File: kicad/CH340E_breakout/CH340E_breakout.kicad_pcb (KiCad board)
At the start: 2 copper layers, 22.7 x 16.7 mm, 27 parts, among them J1 USB-ID, J2 FTDI_PINS_1X06_input, U1 MCP1702-CB, U2 HT42B534-MSOP10

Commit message: schematic and routing completed
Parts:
- removed C10, C9: 47p, SquantorRcl:C_0402
- removed C6: 100n, SquantorRcl:C_0402
- removed R4, R5: 33, SquantorRcl:R_0402_hand
- removed R8: 10K, SquantorRcl:R_0402_hand
- removed SJ1: vddio=vddconn, SquantorSpecial:solder_jumper_2way_noconn
- removed SJ3: vddio=3.3v, SquantorSpecial:solder_jumper_2way_conn
- added R2: 1K, SquantorRcl:R_0402_hand, F.Cu at (152.7, 97.8)
- D2: value D_Schottky -> RED; footprint SquantorDiodes:SOD-523 -> SquantorRcl:R_0603_hand
- U2: value HT42B534-MSOP10 -> CH340E
- moved N1 14.2 mm to (136.4, 86.1)
- moved N2 14.2 mm to (135.3, 90.1)
- moved D2 12.4 mm to (150.0, 97.8)
- moved D1 12.0 mm to (151.7, 85.4)
- moved R6 11.7 mm to (149.5, 85.5), turned to 270 degrees
- moved C7 6.23 mm to (149.9, 89.3), turned to 180 degrees
- moved C4 2.95 mm to (153.3, 95.2)
- moved SJ2 2.95 mm to (150.9, 95.3)
- moved U1 2.95 mm to (150.5, 95.3)
- moved U2 2.86 mm to (150.1, 91.8), turned to 0 degrees
- moved J2 2.60 mm to (157.5, 97.3)
- moved C8 2.23 mm to (152.5, 89.2), turned to 180 degrees
- moved R1 0.81 mm to (147.8, 94.8), turned to 270 degrees
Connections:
- D2 pad 1: /VDD -> /VSS
- D2 pad 2: /VDDIO -> Net-(D2-Pad2)
- U2 pad 1: /VDD -> /USB_DP
- U2 pad 10: Net-(C10-Pad2) -> /VDD_33V
- U2 pad 2: /VDD_33V -> /USB_DM
- U2 pad 4: /CTSI -> /RTSO
- U2 pad 5: /TXO -> /CTSI
- U2 pad 6: /VDDIO -> /ACT
- U2 pad 7: /RXI -> /VDD
- U2 pad 8: /RTSO -> /TXO
- U2 pad 9: Net-(C9-Pad2) -> /RXI
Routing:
- net /ACT: track 0.00 -> 12.6 mm
- net /VDDIO: track 11.2 -> 0.00 mm, vias 2 -> 0
- net /VDDCONN: track 18.3 -> 8.82 mm
- net /VSS: track 20.4 -> 25.3 mm, vias 10 -> 7
- net /VDD_33V: track 6.34 -> 2.36 mm, vias 1 -> 0
- net /RXI: track 17.5 -> 14.0 mm
- net /VDD: track 27.2 -> 24.1 mm
- net Net-(C10-Pad2): track 2.82 -> 0.00 mm
- net Net-(C9-Pad2): track 2.82 -> 0.00 mm
- net /TXO: track 8.71 -> 5.98 mm, vias 0 -> 1
- net /USB_DP: track 2.77 -> 5.33 mm
- net /USB_DM: track 2.79 -> 5.27 mm
- net /CTSI: track 8.98 -> 10.8 mm
- net Net-(D2-Pad2): track 0.00 -> 1.30 mm
- net /RTSO: track 16.7 -> 15.9 mm
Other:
- outline, holes or cut-outs redrawn

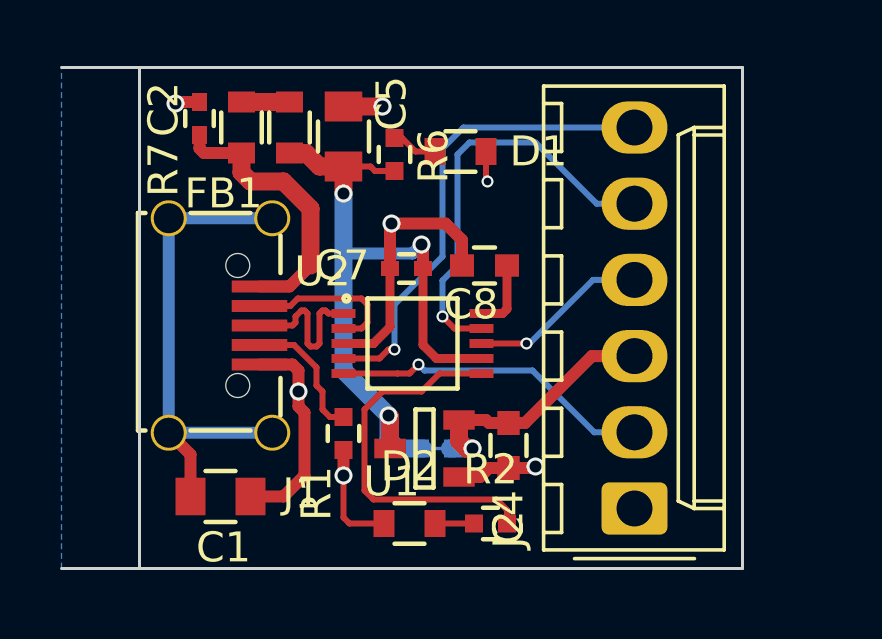
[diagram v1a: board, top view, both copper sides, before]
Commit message: silkscreen layout top completed
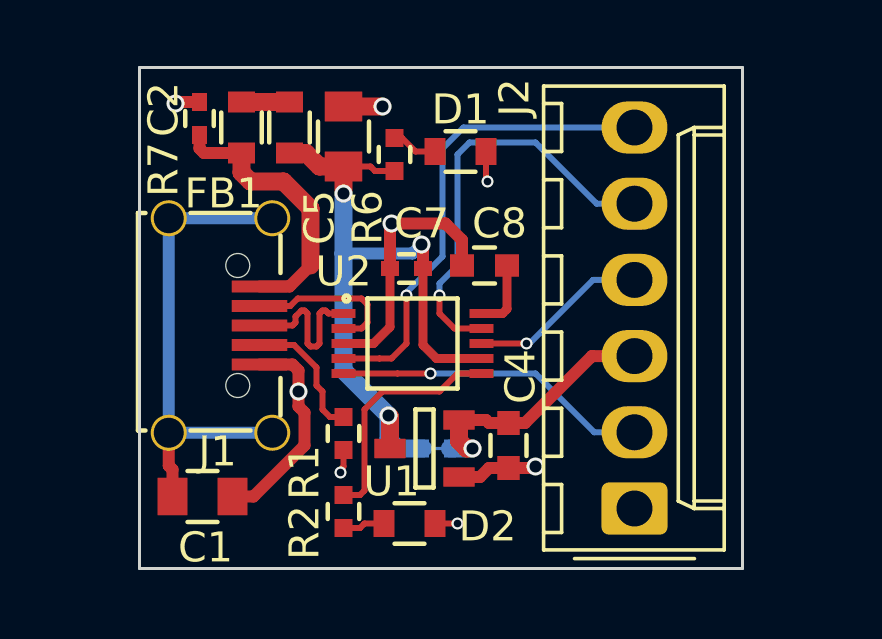
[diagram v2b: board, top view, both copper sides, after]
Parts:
- moved R2 4.92 mm to (147.8, 97.4), turned to 90 degrees
- moved C1 0.60 mm to (143.1, 96.9)
- turned D2 to 180 degrees
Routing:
- net /ACT: track 12.6 -> 7.86 mm
- net /VSS: track 25.3 -> 23.1 mm, vias 7 -> 8
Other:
- board size 22.7 x 16.7 mm -> 20.1 x 16.7 mm

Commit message: further small changes to silk
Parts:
- moved N2 19.7 mm to (154.9, 88.6), turned to 270 degrees
- moved N1 14.6 mm to (150.9, 87.5), turned to 270 degrees
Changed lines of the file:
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@@
     (34 B.Paste user)
     (35 F.Paste user)
-    (36 B.SilkS user hide)
-    (37 F.SilkS user)
+    (36 B.SilkS user)
+    (37 F.SilkS user hide)
     (38 B.Mask user)
     (39 F.Mask user)
@@
   )
   (module Symbols:OSHW-Symbol_6.7x6mm_SilkScreen (layer B.Cu)
-    (at 136.4 86.1 180)
+    (at 150.9 87.5 270)
     (descr "Open Source Hardware Symbol")
     (tags "Logo Symbol OSHW")
     (attr virtual)
-    (fp_text reference N1 (at 0 0 180) (layer B.SilkS) hide
+    (fp_text reference N1 (at 0 0 270) (layer B.SilkS) hide
       (effects (font (size 1 1) (thickness 0.15)) (justify mirror))
     )
-    (fp_text value OHWLOGO (at 0.75 0 180) (layer B.Fab) hide
+    (fp_text value OHWLOGO (at 0.75 0 270) (layer B.Fab) hide
       (effects (font (size 1 1) (thickness 0.15)) (justify mirror))
     )
@@
   )
   (module SquantorLabels:Label_version (layer B.Cu)
-    (at 135.3 90.1 180)
-    (fp_text reference N2 (at 0 -1.4 180) (layer B.Fab) hide
+    (at 154.9 88.6 270)
+    (fp_text reference N2 (at 0 -1.4 270) (layer B.Fab) hide
       (effects (font (size 1 1) (thickness 0.15)) (justify mirror))
     )
-    (fp_text value 20190401 (at -0.4 0.1 180) (layer B.SilkS)
+    (fp_text value 20190401 (at -0.4 0.1 270) (layer B.SilkS)
       (effects (font (size 1 1) (thickness 0.15)) (justify mirror))
     )
-    (fp_text user V: (at -4.8 0.1 180) (layer B.SilkS)
+    (fp_text user V: (at -4.8 0.1 270) (layer B.SilkS)
       (effects (font (size 1 1) (thickness 0.15)) (justify mirror))
     )
@@
       (effects (font (size 1 1) (thickness 0.15)) (justify mirror))
     )
-    (fp_text value vddconn=vdd (at -1.6 -0.6 270) (layer B.SilkS)
+    (fp_text value vddconn=vdd (at -1.7 0.4 270) (layer B.SilkS)
       (effects (font (size 0.8 0.8) (thickness 0.12)) (justify mirror))
     )

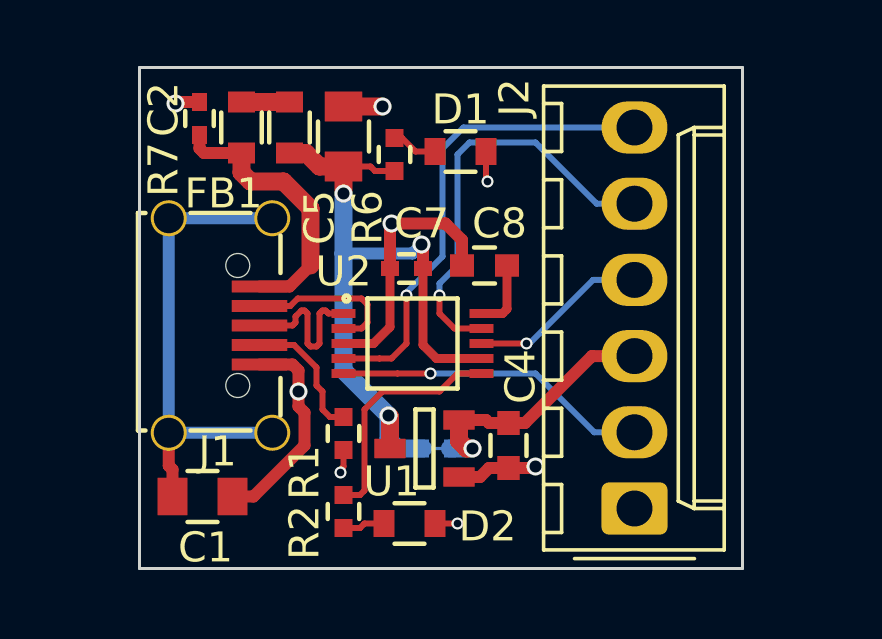
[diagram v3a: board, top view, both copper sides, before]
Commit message: changed LED's to general purpose 0603 diode footprint
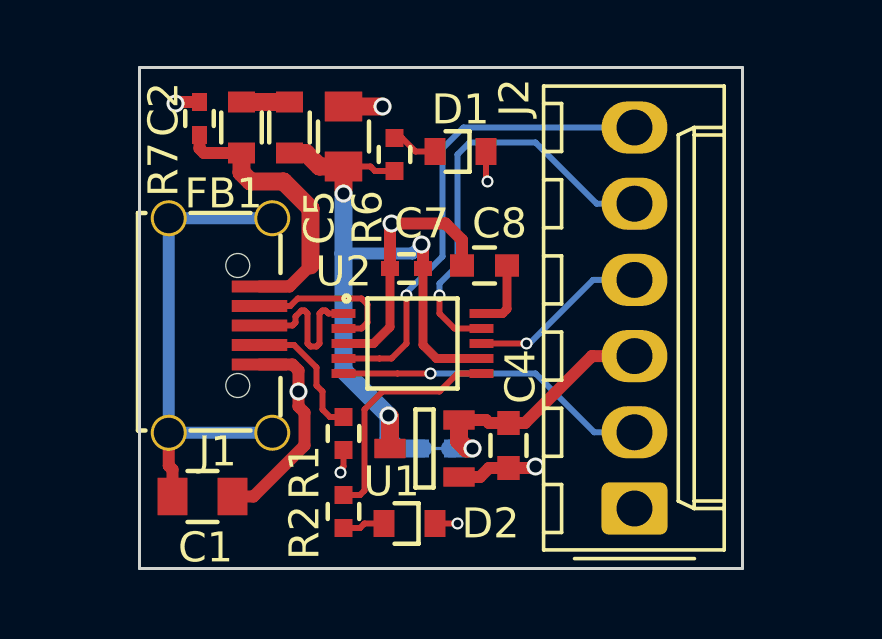
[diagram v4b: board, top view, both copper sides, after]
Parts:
- D1, D2: footprint SquantorRcl:R_0603_hand -> SquantorDiodes:D_0603_hand
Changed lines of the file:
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@@
     (34 B.Paste user)
     (35 F.Paste user)
-    (36 B.SilkS user)
-    (37 F.SilkS user hide)
+    (36 B.SilkS user hide)
+    (37 F.SilkS user)
     (38 B.Mask user)
     (39 F.Mask user)
@@
       (net 4 /VDD))
   )
-  (module SquantorRcl:R_0603_hand (layer F.Cu)
-    (at 151.7 85.4 180)
-    (descr "Resistor SMD 0603, reflow soldering, Vishay (see dcrcw.pdf)")
-    (tags "resistor 0603")
-    (attr smd)
-    (fp_text reference D1 (at 0 1.4) (layer F.SilkS)
-      (effects (font (size 1 1) (thickness 0.15)))
-    )
-    (fp_text value RED (at 0 1.4) (layer F.Fab)
-      (effects (font (size 1 1) (thickness 0.15)))
-    )
-    (fp_line (start -0.5 -0.675) (end 0.5 -0.675) (layer F.SilkS) (width 0.15))
-    (fp_line (start 0.5 0.675) (end -0.5 0.675) (layer F.SilkS) (width 0.15))
-    (fp_line (start 1.5 -0.8) (end 1.5 0.8) (layer F.CrtYd) (width 0.05))
-    (fp_line (start -1.5 -0.8) (end -1.5 0.8) (layer F.CrtYd) (width 0.05))
-    (fp_line (start -1.5 0.8) (end 1.5 0.8) (layer F.CrtYd) (width 0.05))
-    (fp_line (start -1.5 -0.8) (end 1.5 -0.8) (layer F.CrtYd) (width 0.05))
-    (fp_line (start -0.8 -0.4) (end 0.8 -0.4) (layer F.Fab) (width 0.1))
-    (fp_line (start 0.8 -0.4) (end 0.8 0.4) (layer F.Fab) (width 0.1))
-    (fp_line (start 0.8 0.4) (end -0.8 0.4) (layer F.Fab) (width 0.1))
-    (fp_line (start -0.8 0.4) (end -0.8 -0.4) (layer F.Fab) (width 0.1))
-    (pad 2 smd rect (at 0.85 0 180) (size 0.7 0.9) (layers F.Cu F.Paste F.Mask)
-      (net 13 "Net-(D1-Pad2)"))
-    (pad 1 smd rect (at -0.85 0 180) (size 0.7 0.9) (layers F.Cu F.Paste F.Mask)
-      (net 1 /VSS))
-    (model Resistors_SMD.3dshapes/R_0603.wrl
-      (at (xyz 0 0 0))
-      (scale (xyz 1 1 1))
-      (rotate (xyz 0 0 0))
-    )
-  )
   (module SquantorRcl:C_0402 (layer F.Cu)
     (at 143 84.3 90)
@@
       (net 4 /VDD))
     (model Resistors_SMD.3dshapes/R_0402.wrl
-      (at (xyz 0 0 0))
-      (scale (xyz 1 1 1))
-      (rotate (xyz 0 0 0))
-    )
-  )
-  (module SquantorRcl:R_0603_hand (layer F.Cu)
-    (at 150 97.8 180)
-    (descr "Resistor SMD 0603, reflow soldering, Vishay (see dcrcw.pdf)")
-    (tags "resistor 0603")
-    (attr smd)
-    (fp_text reference D2 (at -2.6 -0.1 180) (layer F.SilkS)
-      (effects (font (size 1 1) (thickness 0.15)))
-    )
-    (fp_text value RED (at -2.9 -0.1 180) (layer F.Fab)
-      (effects (font (size 1 1) (thickness 0.15)))
-    )
-    (fp_line (start -0.8 0.4) (end -0.8 -0.4) (layer F.Fab) (width 0.1))
-    (fp_line (start 0.8 0.4) (end -0.8 0.4) (layer F.Fab) (width 0.1))
-    (fp_line (start 0.8 -0.4) (end 0.8 0.4) (layer F.Fab) (width 0.1))
-    (fp_line (start -0.8 -0.4) (end 0.8 -0.4) (layer F.Fab) (width 0.1))
-    (fp_line (start -1.5 -0.8) (end 1.5 -0.8) (layer F.CrtYd) (width 0.05))
-    (fp_line (start -1.5 0.8) (end 1.5 0.8) (layer F.CrtYd) (width 0.05))
-    (fp_line (start -1.5 -0.8) (end -1.5 0.8) (layer F.CrtYd) (width 0.05))
-    (fp_line (start 1.5 -0.8) (end 1.5 0.8) (layer F.CrtYd) (width 0.05))
-    (fp_line (start 0.5 0.675) (end -0.5 0.675) (layer F.SilkS) (width 0.15))
-    (fp_line (start -0.5 -0.675) (end 0.5 -0.675) (layer F.SilkS) (width 0.15))
-    (pad 1 smd rect (at -0.85 0 180) (size 0.7 0.9) (layers F.Cu F.Paste F.Mask)
-      (net 1 /VSS))
-    (pad 2 smd rect (at 0.85 0 180) (size 0.7 0.9) (layers F.Cu F.Paste F.Mask)
-      (net 16 "Net-(D2-Pad2)"))
-    (model Resistors_SMD.3dshapes/R_0603.wrl
       (at (xyz 0 0 0))
       (scale (xyz 1 1 1))
@@
       (net 5 /VDD_33V))
   )
+  (module SquantorDiodes:D_0603_hand (layer F.Cu)
+    (at 151.7 85.4 180)
+    (descr "Diode SMD 0603, reflow soldering, general purpose")
+    (tags "Diode 0603")
+    (attr smd)
+    (fp_text reference D1 (at 0 1.4 180) (layer F.SilkS)
+      (effects (font (size 1 1) (thickness 0.15)))
+    )
+    (fp_text value RED (at -0.1 1.4 180) (layer F.Fab)
+      (effects (font (size 1 1) (thickness 0.15)))
+    )
+    (fp_line (start -0.8 0.4) (end -0.8 -0.4) (layer F.Fab) (width 0.1))
+    (fp_line (start 0.8 0.4) (end -0.8 0.4) (layer F.Fab) (width 0.1))
+    (fp_line (start 0.8 -0.4) (end 0.8 0.4) (layer F.Fab) (width 0.1))
+    (fp_line (start -0.8 -0.4) (end 0.8 -0.4) (layer F.Fab) (width 0.1))
+    (fp_line (start -1.5 -0.8) (end 1.5 -0.8) (layer F.CrtYd) (width 0.05))
+    (fp_line (start -1.5 0.8) (end 1.5 0.8) (layer F.CrtYd) (width 0.05))
+    (fp_line (start -1.5 -0.8) (end -1.5 0.8) (layer F.CrtYd) (width 0.05))
+    (fp_line (start 1.5 -0.8) (end 1.5 0.8) (layer F.CrtYd) (width 0.05))
+    (fp_line (start 0.5 0.675) (end -0.3 0.675) (layer F.SilkS) (width 0.15))
+    (fp_line (start -0.3 -0.675) (end 0.5 -0.675) (layer F.SilkS) (width 0.15))
+    (fp_line (start -0.3 -0.675) (end -0.3 0.675) (layer F.SilkS) (width 0.15))
+    (pad 1 smd rect (at -0.85 0 180) (size 0.7 0.9) (layers F.Cu F.Paste F.Mask)
+      (net 1 /VSS))
+    (pad 2 smd rect (at 0.85 0 180) (size 0.7 0.9) (layers F.Cu F.Paste F.Mask)
+      (net 13 "Net-(D1-Pad2)"))
+  )
+  (module SquantorDiodes:D_0603_hand (layer F.Cu)
+    (at 150 97.8 180)
+    (descr "Diode SMD 0603, reflow soldering, general purpose")
+    (tags "Diode 0603")
+    (attr smd)
+    (fp_text reference D2 (at -2.7 0 180) (layer F.SilkS)
+      (effects (font (size 1 1) (thickness 0.15)))
+    )
+    (fp_text value RED (at -2.7 0 180) (layer F.Fab)
+      (effects (font (size 1 1) (thickness 0.15)))
+    )
+    (fp_line (start -0.3 -0.675) (end -0.3 0.675) (layer F.SilkS) (width 0.15))
+    (fp_line (start -0.3 -0.675) (end 0.5 -0.675) (layer F.SilkS) (width 0.15))
+    (fp_line (start 0.5 0.675) (end -0.3 0.675) (layer F.SilkS) (width 0.15))
+    (fp_line (start 1.5 -0.8) (end 1.5 0.8) (layer F.CrtYd) (width 0.05))
+    (fp_line (start -1.5 -0.8) (end -1.5 0.8) (layer F.CrtYd) (width 0.05))
+    (fp_line (start -1.5 0.8) (end 1.5 0.8) (layer F.CrtYd) (width 0.05))
+    (fp_line (start -1.5 -0.8) (end 1.5 -0.8) (layer F.CrtYd) (width 0.05))
+    (fp_line (start -0.8 -0.4) (end 0.8 -0.4) (layer F.Fab) (width 0.1))
+    (fp_line (start 0.8 -0.4) (end 0.8 0.4) (layer F.Fab) (width 0.1))
+    (fp_line (start 0.8 0.4) (end -0.8 0.4) (layer F.Fab) (width 0.1))
+    (fp_line (start -0.8 0.4) (end -0.8 -0.4) (layer F.Fab) (width 0.1))
+    (pad 2 smd rect (at 0.85 0 180) (size 0.7 0.9) (layers F.Cu F.Paste F.Mask)
+      (net 16 "Net-(D2-Pad2)"))
+    (pad 1 smd rect (at -0.85 0 180) (size 0.7 0.9) (layers F.Cu F.Paste F.Mask)
+      (net 1 /VSS))
+  )
   (gr_line (start 141 82.6) (end 161.1 82.6) (layer Edge.Cuts) (width 0.1))

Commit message: added labeled UART connector
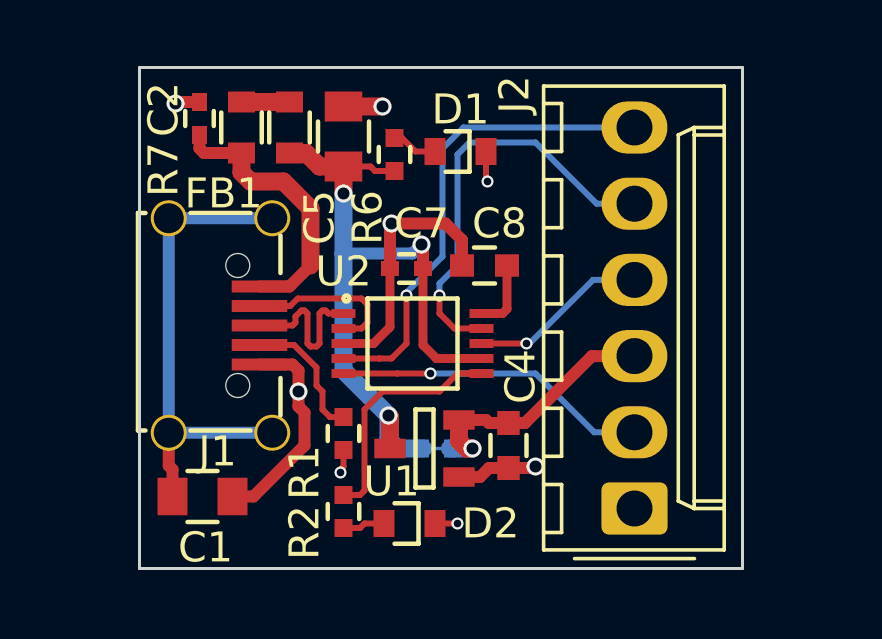
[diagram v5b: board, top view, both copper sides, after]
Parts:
- J2: footprint Connector_Molex:Molex_KK-254_AE-6410-06A_1x06_P2.54mm_Vertical -> SquantorConnectorsNamed:Molex_KK-254_AE-6410-06A_1x06_P2.54mm_Vertical_FTDI_UART
- moved N1 7.74 mm to (144.1, 91.2)
- moved N2 7.74 mm to (148.1, 92.3)
